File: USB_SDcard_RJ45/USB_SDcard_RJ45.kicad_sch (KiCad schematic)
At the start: 0 parts

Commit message: Add CH339F symbol
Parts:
- added U2: ~, Package_DFN_QFN:QFN-32-1EP_4x4mm_P0.4mm_EP2.65x2.65mm_ThermalVias, symbol 3in1lib:CH339F
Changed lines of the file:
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@@
 	(generator_version "9.0")
 	(paper "A4")
+	(symbol
+		(lib_name "CH339F_1")
+		(lib_id "3in1lib:CH339F")
+		(at 102.87 77.47 0)
+		(unit 1)
+		(exclude_from_sim no)
+		(in_bom yes)
+		(on_board yes)
+		(dnp no)
+		(fields_autoplaced yes)
+		(property "Reference" "U2"
+			(at 158.75 81.2098 0)
+			(effects
+				(font
+					(size 1.27 1.27)
+				)
+			)
+		)
+		(property "Value" "~"
+			(at 158.75 83.7498 0)
+			(effects
+				(font
+					(size 1.27 1.27)
+				)
+			)
+		)
+		(property "Footprint" "Package_DFN_QFN:QFN-32-1EP_4x4mm_P0.4mm_EP2.65x2.65mm_ThermalVias"
+			(at 102.87 77.47 0)
+			(effects
+				(font
+					(size 1.27 1.27)
+				)
+				(hide yes)
+			)
+		)
+		(property "Datasheet" ""
+			(at 102.87 77.47 0)
+			(effects
+				(font
+					(size 1.27 1.27)
+				)
+				(hide yes)
+			)
+		)
+		(property "Description" ""
+			(at 102.87 77.47 0)
+			(effects
+				(font
+					(size 1.27 1.27)
+				)
+				(hide yes)
+			)
+		)
+		(pin "26"
+		)
+		(pin "25"
+		)
+		(pin "9"
+		)
+		(pin "10"
+		)
+		(pin "15"
+		)
+		(pin "14"
+		)
+		(pin "13"
+		)
+		(pin "12"
+		)
+		(pin "8"
+		)
+		(pin "16"
+		)
+		(pin "5"
+		)
+		(pin "19"
+		)
+		(pin "6"
+		)
+		(pin "18"
+		)
+		(pin "11"
+		)
+		(pin "20"
+		)
+		(pin "1"
+		)
+		(pin "23"
+		)
+		(pin "2"
+		)
+		(pin "22"
+		)
+		(pin "7"
+		)
+		(pin "17"
+		)
+		(pin "4"
+		)
+		(pin "24"
+		)
+		(pin "27"
+		)
+		(pin "3"
+		)
+		(pin "21"
+		)
+		(pin "33"
+		)
+		(pin "32"
+		)
+		(pin "28"
+		)
+		(pin "31"
+		)
+		(pin "29"
+		)
+		(pin "30"
+		)
+		(instances
+			(project ""
+				(path "/6ae37710-dc5d-4d7d-8394-89e891506da0"
+					(reference "U2")
+					(unit 1)
+				)
+			)
+		)
+	)
 	(sheet_instances
 		(path "/"

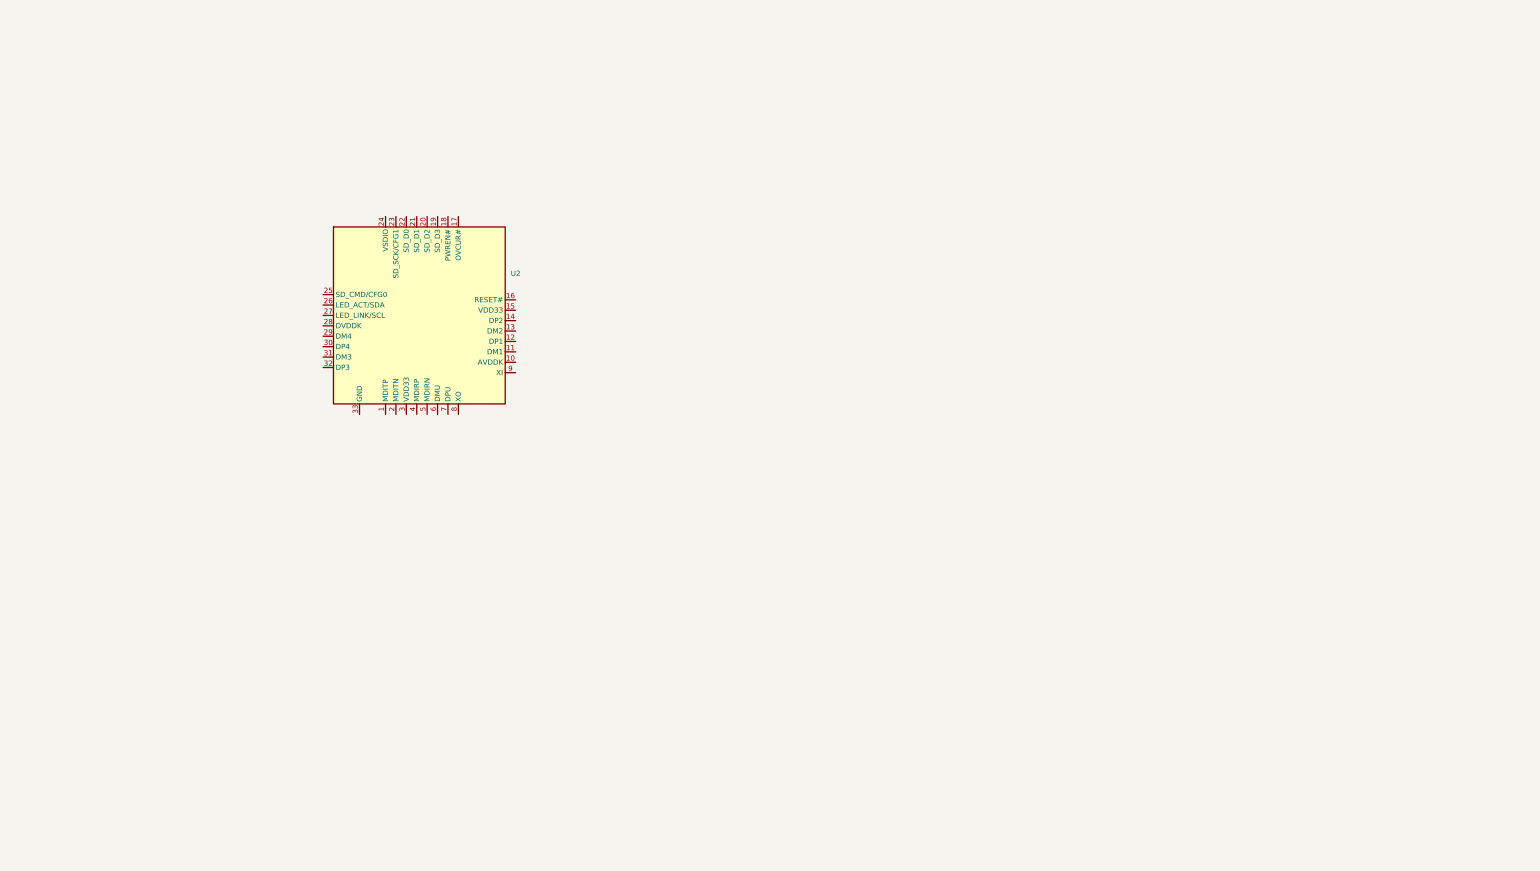
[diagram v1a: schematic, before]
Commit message: Add USB stack and rj45 port
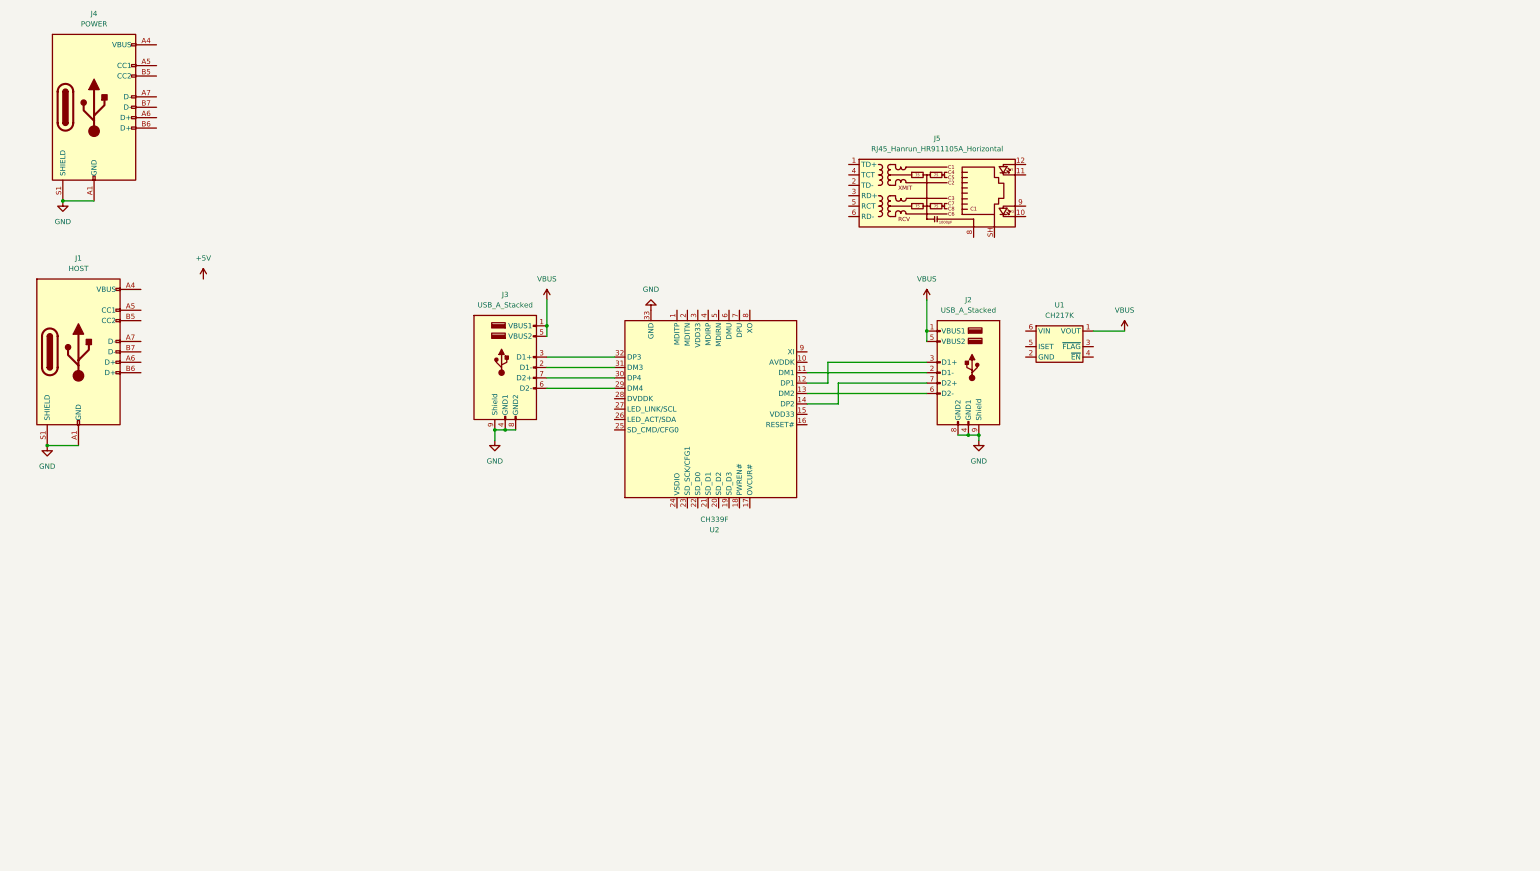
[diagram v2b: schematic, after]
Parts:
- added J1: HOST, symbol Connector:USB_C_Receptacle_USB2.0_14P
- added J2, J3: USB_A_Stacked, Connector_USB:USB_A_CUI_UJ2-ADH-TH_Horizontal_Stacked, symbol Connector:USB_A_Stacked
- added J4: POWER, symbol Connector:USB_C_Receptacle_USB2.0_14P
- added J5: RJ45_Hanrun_HR911105A_Horizontal, Connector_RJ:RJ45_Hanrun_HR911105A_Horizontal, symbol Connector:RJ45_Hanrun_HR911105A_Horizontal
- added U1: CH217K, Package_TO_SOT_SMD:SOT-23-6, symbol 3in1lib:CH217K
- U2: value ~ -> CH339F
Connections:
- net at U2.11 (DM1): now also J2.2 (D1-)
- net at U2.12 (DP1): now also J2.3 (D1+)
- net at U2.13 (DM2): now also J2.6 (D2-)
- net at U2.14 (DP2): now also J2.7 (D2+)
- net at U2.29 (DM4): now also J3.6 (D2-)
- net at U2.30 (DP4): now also J3.7 (D2+)
- net at U2.31 (DM3): now also J3.2 (D1-)
- net at U2.32 (DP3): now also J3.3 (D1+)
- net GND: now reaches U2.33 (GND)
- net GND: now also J1.A1 (GND), J1.A12 (GND), J1.B1 (GND), J1.B12 (GND), J1.S1 (SHIELD), J2.4 (GND1), J2.8 (GND2), J2.9 (Shield), J3.4 (GND1), J3.8 (GND2), J3.9 (Shield), J4.A1 (GND), J4.A12 (GND), J4.B1 (GND), J4.B12 (GND), J4.S1 (SHIELD)
- new net: J1.A4 (VBUS), J1.A9 (VBUS), J1.B4 (VBUS), J1.B9 (VBUS)
- new net: J4.A4 (VBUS), J4.A9 (VBUS), J4.B4 (VBUS), J4.B9 (VBUS)
- new net VBUS: J2.1 (VBUS1), J2.5 (VBUS2), J3.1 (VBUS1), J3.5 (VBUS2), U1.1 (VOUT)
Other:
- moved on the sheet: U2

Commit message: Add components to schematic
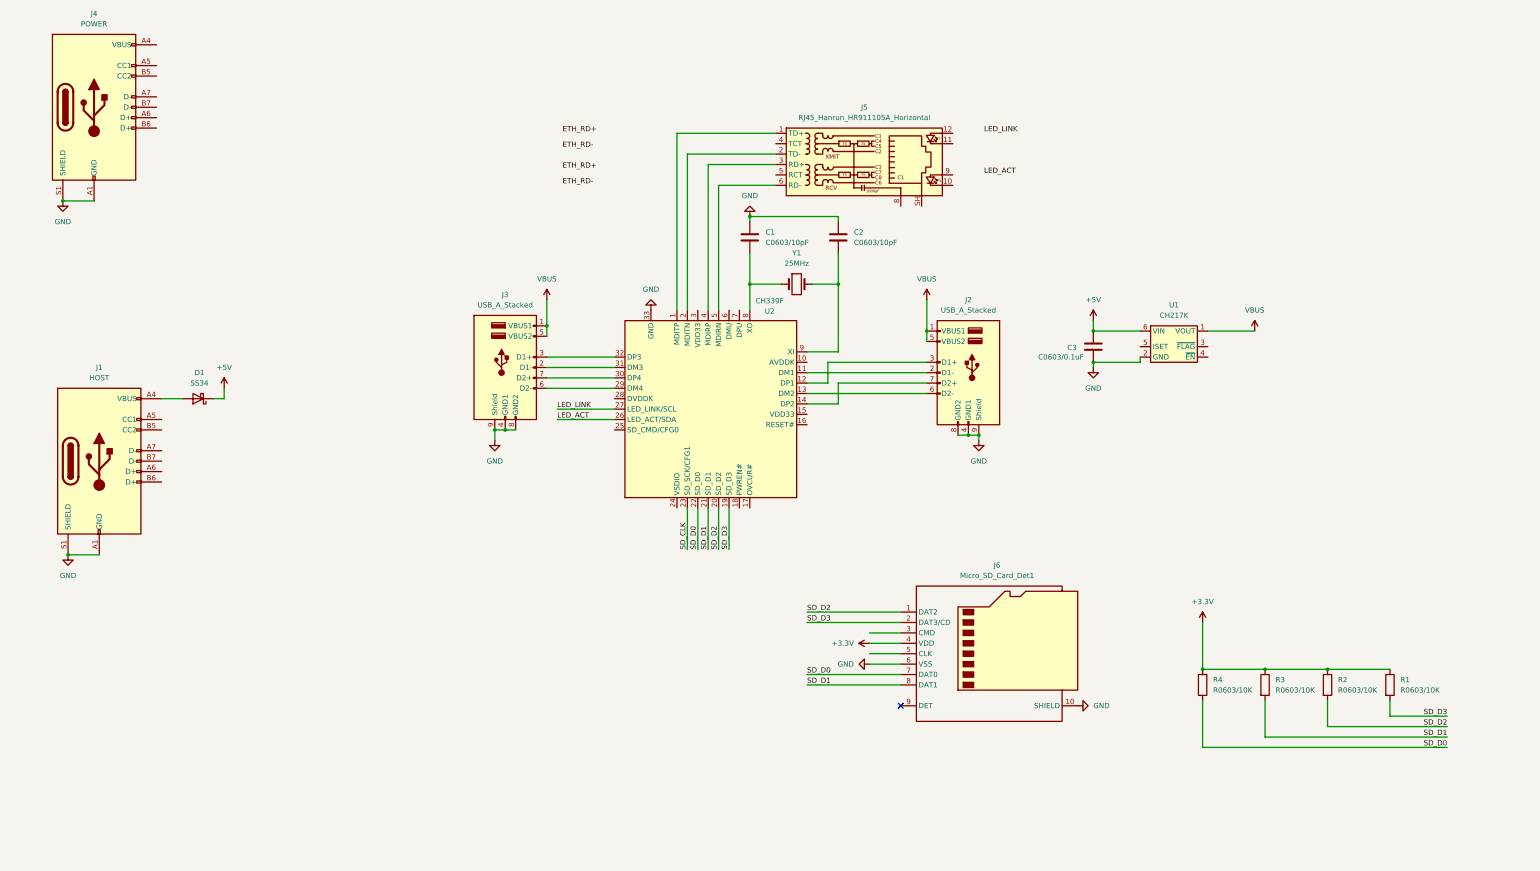
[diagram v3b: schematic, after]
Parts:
- added C1, C2: C0603/10pF, symbol Device:C
- added C3: C0603/0.1uF, symbol Device:C
- added D1: SS34, Diode_SMD:D_SMA, symbol Diode:SS34
- added J6: Micro_SD_Card_Det1, 3in1:MiSD-PP-9P-V2, symbol Connector:Micro_SD_Card_Det1
- added R1, R2, R3, R4: R0603/10K, symbol Device:R
- added Y1: 25MHz, symbol Device:Crystal
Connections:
- net +5V: now also U1.6 (VIN), C3.1, D1.1 (K)
- net GND: now also U1.2 (GND), C1.1, C2.1, C3.2, J6.10 (SHIELD), J6.6 (VSS)
- net at J5.1 (TD+): now also U2.1 (MDITP)
- net at J5.2 (TD-): now also U2.2 (MDITN)
- net at J5.3 (RD+): now also U2.4 (MDIRP)
- net at J5.6 (RD-): now also U2.5 (MDIRN)
- net at J1.A4 (VBUS), J1.A9 (VBUS), J1.B4 (VBUS)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: now also D1.2 (A)
- net SD_D3: now reaches U2.19 (SD_D3)
- net SD_D3: now also J6.2 (DAT3/CD), R1.2
- net SD_D2: now reaches U2.20 (SD_D2)
- net SD_D2: now also J6.1 (DAT2), R2.2
- net SD_D1: now reaches U2.21 (SD_D1)
- net SD_D1: now also J6.8 (DAT1), R3.2
- net SD_D0: now reaches U2.22 (SD_D0)
- net SD_D0: now also J6.7 (DAT0), R4.2
- net SD_CLK: now reaches U2.23 (SD_SCK/CFG1)
- net LED_ACT: now reaches U2.26 (LED_ACT/SDA)
- net LED_LINK: now reaches U2.27 (LED_LINK/SCL)
- net at U2.8 (XO): now also C1.2, Y1.1
- net at U2.9 (XI): now also C2.2, Y1.2
- new net +3.3V: J6.4 (VDD), R1.1, R2.1, R3.1, R4.1
- no-connect marks 0 -> 1
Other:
- moved on the sheet: J1, J5, U1

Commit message: Add CH339 datasheet
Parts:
- added R5, R6: R0603/4K7, symbol Device:R
- added R7: R0603/100K, symbol Device:R
- added R8: R0603/10k, symbol Device:R
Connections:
- net +5V: now also R8.2
- net GND: now also R5.2, R6.2, R7.1; no longer J1.S1 (SHIELD)
- net SD_CLK: now also J6.5 (CLK)
- net at J1.A5 (CC1): now also R5.1
- net HOST_DP: now reaches J1.A6 (D+)
- net HOST_DP: now also J1.B6 (D+), U2.7 (DPU)
- net HOST_DN: now reaches J1.A7 (D-)
- net HOST_DN: now also J1.B7 (D-), U2.6 (DMU)
- net at J1.B5 (CC2): now also R6.1
- net OVCUR#: now reaches U2.17 (OVCUR#)
- net OVCUR#: now also U1.3 (~{FLAG}), R8.1
- net EN: now reaches U2.18 (PWREN#)
- new net: J1.S1 (SHIELD), R7.2
- no-connect marks 1 -> 2
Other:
- moved on the sheet: C3, D1, J1, R1, R2, R3, R4

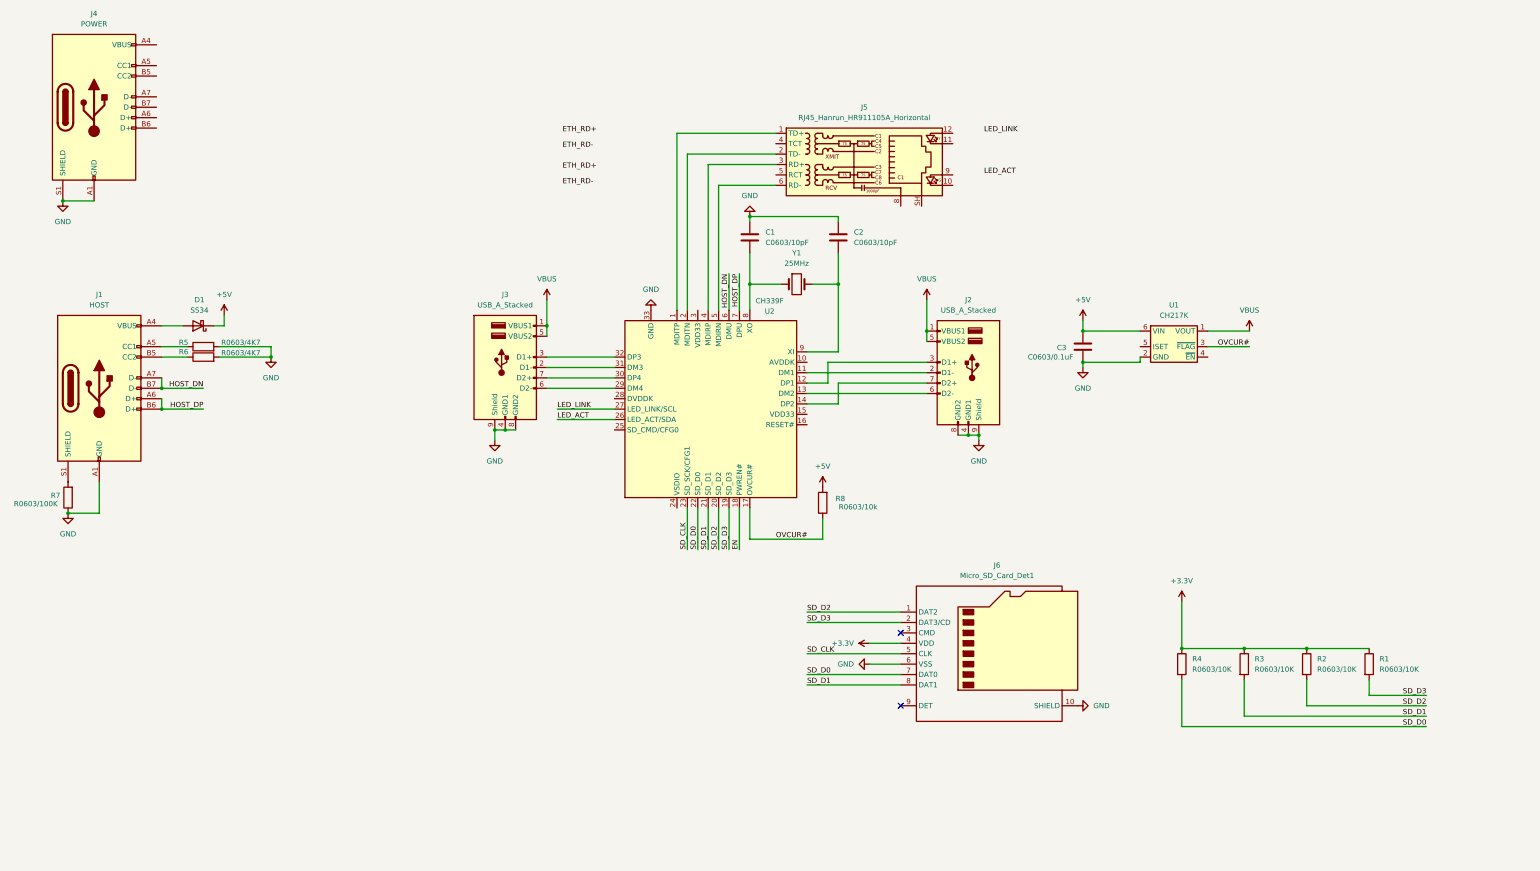
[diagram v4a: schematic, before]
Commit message: Change to CH339W hub ic
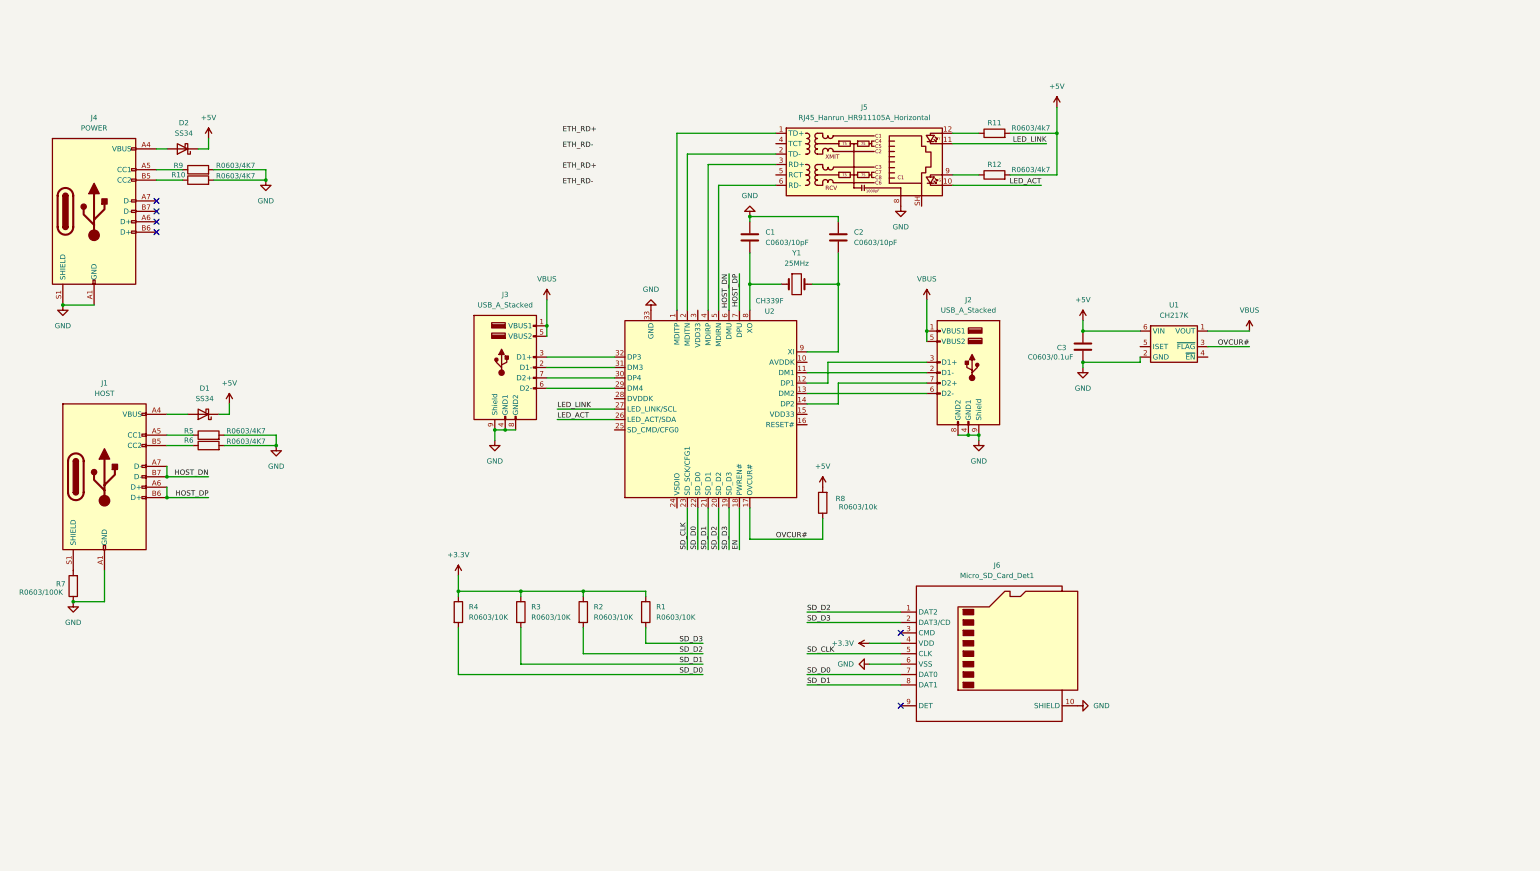
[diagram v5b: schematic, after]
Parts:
- added D2: SS34, Diode_SMD:D_SMA, symbol Diode:SS34
- added R10, R9: R0603/4K7, symbol Device:R
- added R11, R12: R0603/4k7, symbol Device:R
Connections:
- net +5V: now also D2.1 (K), R11.2, R12.2
- net GND: now also J5.8, R10.2, R9.2
- net LED_ACT: now also J5.10
- net LED_LINK: now also J5.11
- net at J5.12: now also R11.1
- net at J5.9: now also R12.1
- net at J4.A4 (VBUS), J4.A9 (VBUS), J4.B4 (VBUS)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: now also D2.2 (A)
- net at J4.A5 (CC1): now also R9.1
- net at J4.B5 (CC2): now also R10.1
- no-connect marks 2 -> 6
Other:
- moved on the sheet: D1, J1, J4, R1, R2, R3, R4, R5, R6, R7
